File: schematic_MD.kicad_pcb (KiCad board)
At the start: 2 copper layers, 100 x 100 mm, 115 parts, among them J1 XT60, J10 Gate_PWR_Jump, J13 EXPWR_GND, J2 XT60, J3 XT60, J4 CAN_Bus, J5 Rotaly_encoder_1, J6 Rotaly_encoder_2, J7 Z_jumper, J8 Z_jumper, J9 Conn_02x01, Q1 SQJ886EP-T1_GE3, Q2 SQJ886EP-T1_GE3, Q3 SQJ886EP-T1_GE3, Q4 SQJ886EP-T1_GE3, Q5 SQJ886EP-T1_GE3, Q6 SQJ886EP-T1_GE3, Q7 SQJ886EP-T1_GE3, Q8 SQJ886EP-T1_GE3, SW1 SW_MEC_5G, U1 UCC21520DW, U11 74HC04, U2 XC6206P332MR-G, U3 UCC21520DW, U4 UCC21520DW, U5 UCC21520DW, U6 STM32F405RGTx, U7 MAX3051, U8 L78M05ABDT-TR

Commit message: fix drive circuit
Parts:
- added C26: 10u, Capacitor_SMD:C_1210_3225Metric_Pad1.33x2.70mm_HandSolder, F.Cu at (180.1, 55.6)
- added C43: 1uF, Capacitor_SMD:C_0603_1608Metric_Pad1.08x0.95mm_HandSolder, F.Cu at (182.8, 55.6)
- R24, R25, R26, R27, R28, R29, R30, R31: value 10k -> 20k
- moved U11 2.82 mm to (119.8, 98.2)
- moved C13 2.82 mm to (119.5, 103.4)
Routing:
- net Net-(U5-OUTA): track 0.00 -> 32.2 mm, vias 0 -> 2
- net /Driver1/H-bridge_left: track 11.2 -> 26.8 mm, vias 36 -> 37
- net /Driver1/H-bridge_right: track 7.60 -> 22.9 mm, vias 36 -> 37
- net GND2: track 35.5 -> 44.6 mm, vias 2 -> 6
- net Net-(U3-OUTA): track 31.0 -> 32.4 mm
- net /Driver/H-bridge_right: track 25.8 -> 24.7 mm
- net /Driver/H-bridge_left: track 30.4 -> 29.5 mm

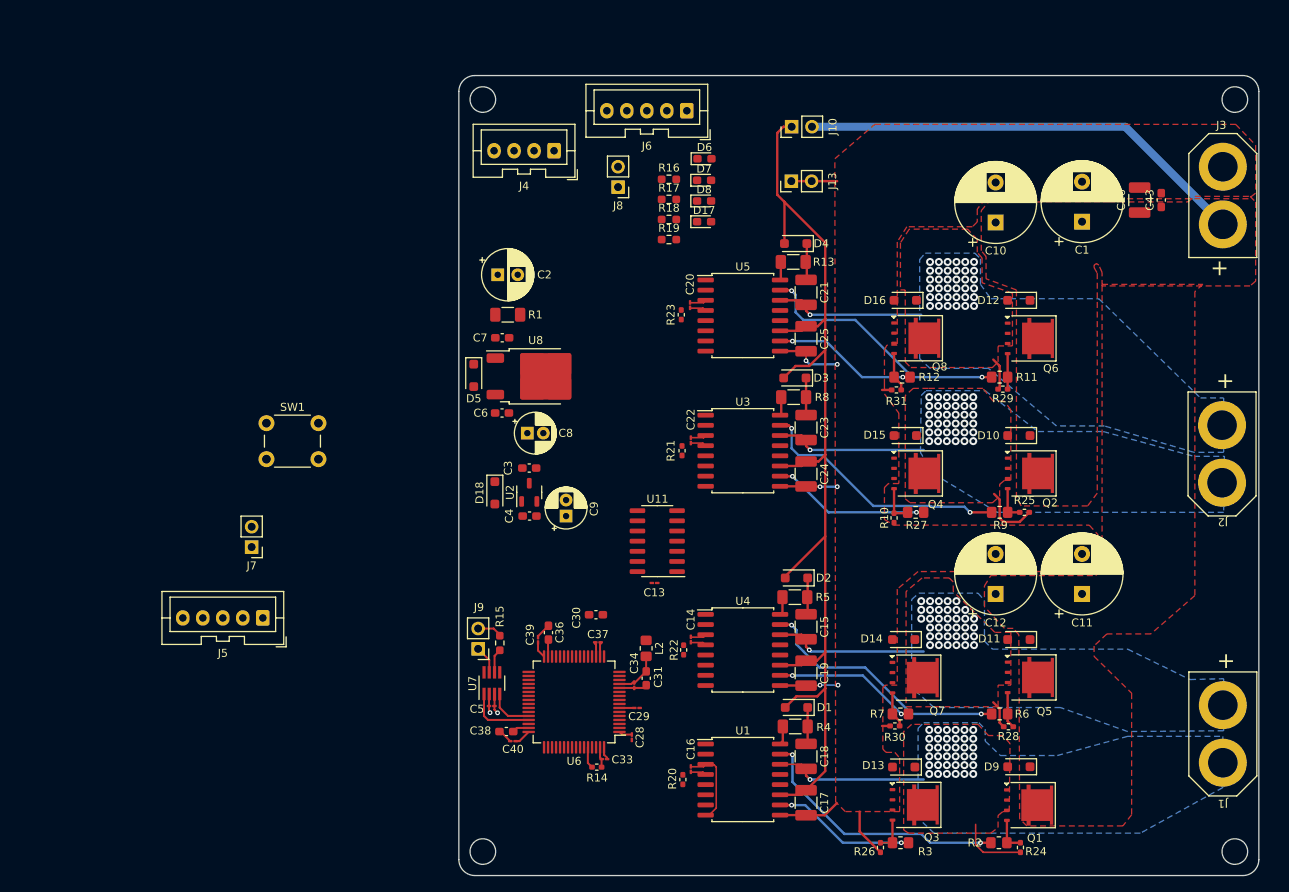
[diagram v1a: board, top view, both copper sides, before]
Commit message: add logic parts
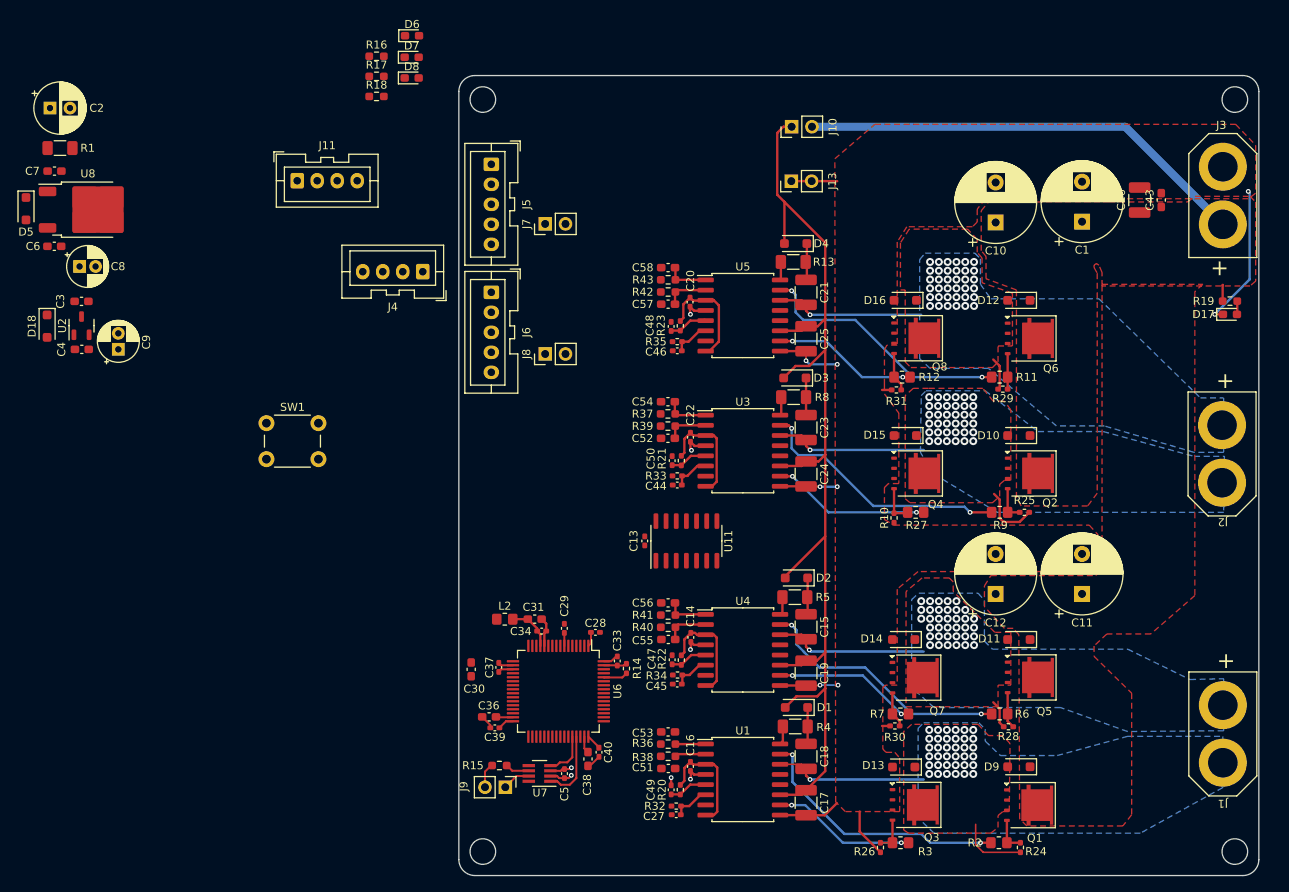
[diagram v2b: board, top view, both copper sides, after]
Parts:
- added C27: 1nF, Capacitor_SMD:C_0402_1005Metric_Pad0.74x0.62mm_HandSolder, F.Cu at (122.2, 132.4)
- added C44: 1nF, Capacitor_SMD:C_0402_1005Metric_Pad0.74x0.62mm_HandSolder, F.Cu at (122.3, 91.2)
- added C45: 1nF, Capacitor_SMD:C_0402_1005Metric_Pad0.74x0.62mm_HandSolder, F.Cu at (122.3, 116.1)
- added C46: 1nF, Capacitor_SMD:C_0402_1005Metric_Pad0.74x0.62mm_HandSolder, F.Cu at (122.3, 74.4)
- added C47: 22nF, Capacitor_SMD:C_0402_1005Metric_Pad0.74x0.62mm_HandSolder, F.Cu at (121.7, 113.0)
- added C48: 22nF, Capacitor_SMD:C_0402_1005Metric_Pad0.74x0.62mm_HandSolder, F.Cu at (121.5, 71.4)
- added C49: 22nF, Capacitor_SMD:C_0402_1005Metric_Pad0.74x0.62mm_HandSolder, F.Cu at (121.5, 129.3)
- added C50: 22nF, Capacitor_SMD:C_0402_1005Metric_Pad0.74x0.62mm_HandSolder, F.Cu at (121.7, 88.1)
- added C51: 33pF, Capacitor_SMD:C_0603_1608Metric_Pad1.08x0.95mm_HandSolder, F.Cu at (121.2, 126.6)
- added C52: 33pF, Capacitor_SMD:C_0603_1608Metric_Pad1.08x0.95mm_HandSolder, F.Cu at (121.1, 85.3)
- added C53: 33pF, Capacitor_SMD:C_0603_1608Metric_Pad1.08x0.95mm_HandSolder, F.Cu at (121.2, 122.0)
- added C54: 33pF, Capacitor_SMD:C_0603_1608Metric_Pad1.08x0.95mm_HandSolder, F.Cu at (121.1, 80.8)
- added C55: 33pF, Capacitor_SMD:C_0603_1608Metric_Pad1.08x0.95mm_HandSolder, F.Cu at (121.2, 110.5)
- added C56: 33pF, Capacitor_SMD:C_0603_1608Metric_Pad1.08x0.95mm_HandSolder, F.Cu at (121.2, 105.9)
- added C57: 33pF, Capacitor_SMD:C_0603_1608Metric_Pad1.08x0.95mm_HandSolder, F.Cu at (121.2, 68.6)
- added C58: 33pF, Capacitor_SMD:C_0603_1608Metric_Pad1.08x0.95mm_HandSolder, F.Cu at (121.2, 64.0)
- added J11: CAN_Bus, Connector_JST:JST_XA_B04B-XASK-1_1x04_P2.50mm_Vertical, F.Cu at (74.8, 53.1)
- added R32: 20k, Resistor_SMD:R_0402_1005Metric_Pad0.72x0.64mm_HandSolder, F.Cu at (122.2, 131.3)
- added R33: 20k, Resistor_SMD:R_0402_1005Metric_Pad0.72x0.64mm_HandSolder, F.Cu at (122.3, 90.0)
- added R34: 20k, Resistor_SMD:R_0402_1005Metric_Pad0.72x0.64mm_HandSolder, F.Cu at (122.3, 114.9)
- added R35: 20k, Resistor_SMD:R_0402_1005Metric_Pad0.72x0.64mm_HandSolder, F.Cu at (122.3, 73.3)
- added R36: 51, Resistor_SMD:R_0603_1608Metric_Pad0.98x0.95mm_HandSolder, F.Cu at (121.2, 123.6)
- added R37: 51, Resistor_SMD:R_0603_1608Metric_Pad0.98x0.95mm_HandSolder, F.Cu at (121.1, 82.3)
- added R38: 51, Resistor_SMD:R_0603_1608Metric_Pad0.98x0.95mm_HandSolder, F.Cu at (121.2, 125.1)
- added R39: 51, Resistor_SMD:R_0603_1608Metric_Pad0.98x0.95mm_HandSolder, F.Cu at (121.1, 83.8)
- added R40: 51, Resistor_SMD:R_0603_1608Metric_Pad0.98x0.95mm_HandSolder, F.Cu at (121.2, 109.0)
- added R41: 51, Resistor_SMD:R_0603_1608Metric_Pad0.98x0.95mm_HandSolder, F.Cu at (121.2, 107.4)
- added R42: 51, Resistor_SMD:R_0603_1608Metric_Pad0.98x0.95mm_HandSolder, F.Cu at (121.2, 67.1)
- added R43: 51, Resistor_SMD:R_0603_1608Metric_Pad0.98x0.95mm_HandSolder, F.Cu at (121.2, 65.5)
- C13, C14, C16, C20, C22, C28, C29, C33, C34, C37, C39, C40, C5: footprint Capacitor_SMD:C_01005_0402Metric_Pad0.57x0.30mm_HandSolder -> Capacitor_SMD:C_0402_1005Metric_Pad0.74x0.62mm_HandSolder
- moved R19 70.5 mm to (191.4, 68.2)
- moved D17 66.7 mm to (191.4, 69.8)
- moved J5 63.5 mm to (99.1, 51.1), turned to -90 degrees
- moved C2 59.7 mm to (43.9, 44.1)
- moved C4 59.7 mm to (47.9, 74.2)
- moved C9 59.7 mm to (52.4, 74.2)
- moved R1 59.7 mm to (45.1, 49.1)
- moved C6 59.7 mm to (44.4, 61.3)
- moved C7 59.7 mm to (44.5, 51.9)
- moved C8 59.7 mm to (47.6, 63.9)
- moved D18 59.7 mm to (43.5, 71.3)
- moved D5 59.7 mm to (40.9, 56.6)
- moved C3 59.7 mm to (47.8, 68.2)
- moved U2 59.7 mm to (47.8, 71.3)
- moved U8 59.7 mm to (48.6, 56.8)
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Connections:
- J4 pad 1: +12V -> GND1
- J4 pad 2: GND1 -> +12V
- U1 pad 1: /Driver/Left_Highside_PWM_IN -> Net-(U1-INA)
- U1 pad 2: /Driver/Left_Lowside_PWM_IN -> Net-(U1-INB)
- U1 pad 6: unconnected-(U1-DT-Pad6) -> Net-(U1-DT)
- U3 pad 1: /Driver1/Left_Highside_PWM_IN -> Net-(U3-INA)
- U3 pad 2: /Driver1/Left_Lowside_PWM_IN -> Net-(U3-INB)
- U3 pad 6: unconnected-(U3-DT-Pad6) -> Net-(U3-DT)
- U4 pad 1: /Driver/Right_Highside_PWM_IN -> Net-(U4-INA)
- U4 pad 2: /Driver/Right_Lowside_PWM_IN -> Net-(U4-INB)
- U4 pad 6: unconnected-(U4-DT-Pad6) -> Net-(U4-DT)
- U5 pad 1: /Driver1/Right_Highside_PWM_IN -> Net-(U5-INA)
- U5 pad 2: /Driver1/Right_Lowside_PWM_IN -> Net-(U5-INB)
- U5 pad 6: unconnected-(U5-DT-Pad6) -> Net-(U5-DT)
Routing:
- net +3.3V: track 27.3 -> 67.7 mm
- net GND2: track 44.6 -> 62.9 mm, vias 6 -> 8
- net GND1: track 21.3 -> 27.2 mm, vias 1 -> 6
- net Net-(U4-INB): track 0.00 -> 5.45 mm
- net Net-(U5-INB): track 0.00 -> 5.42 mm
- net Net-(U3-INA): track 0.00 -> 5.41 mm
- net Net-(U3-INB): track 0.00 -> 5.39 mm
- net Net-(U4-INA): track 0.00 -> 5.36 mm
- net Net-(U5-INA): track 0.00 -> 5.33 mm
- net /Driver1/EN_right: track 0.00 -> 5.04 mm
- net /Driver/EN_right: track 0.00 -> 4.90 mm
- net Net-(U1-DT): track 0.00 -> 4.86 mm
- net /Driver/EN_left: track 0.00 -> 4.83 mm
- net /Driver1/EN_left: track 0.00 -> 4.75 mm
- net Net-(U5-DT): track 0.00 -> 4.63 mm
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
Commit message: update pcb
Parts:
- added Y3: Crystal, Crystal:Crystal_SMD_3225-4Pin_3.2x2.5mm, F.Cu at (105.3, 101.0)
- added Y4: Crystal, Crystal:Crystal_SMD_3215-2Pin_3.2x1.5mm, F.Cu at (110.4, 80.4)
- moved C6 67.6 mm to (111.9, 57.5)
- moved C7 67.6 mm to (112.0, 48.1)
- moved D5 67.6 mm to (108.4, 52.8)
- moved U8 67.6 mm to (116.1, 52.9)
- moved R1 67.6 mm to (112.7, 46.1)
- moved D18 65.8 mm to (108.9, 63.4)
- moved C4 64.5 mm to (111.8, 66.1)
- moved U2 64.5 mm to (111.8, 63.2)
- moved C3 64.5 mm to (111.8, 60.3)
- moved C2 62.7 mm to (106.6, 46.2), turned to 90 degrees
- moved C8 61.1 mm to (108.4, 58.1), turned to 180 degrees
- moved C9 60.5 mm to (112.8, 69.9), turned to 180 degrees
- moved J9 54.3 mm to (110.7, 75.6), turned to 90 degrees
- moved J6 51.3 mm to (99.1, 118.4)
- moved J7 51.3 mm to (105.8, 109.9)
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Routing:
- net Net-(J11-Pin_3): track 3.04 -> 23.1 mm
- net Net-(J11-Pin_4): track 3.58 -> 18.2 mm
- net +3.3V: track 67.7 -> 70.5 mm
- net Net-(U6-BOOT0): track 3.06 -> 1.89 mm

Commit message: fix logic
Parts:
- removed J7, J8: Z_jumper, Connector_PinHeader_2.54mm:PinHeader_1x02_P2.54mm_Vertical
- removed Y3: Crystal, Crystal:Crystal_SMD_3225-4Pin_3.2x2.5mm
- added C32: 18pF, Capacitor_SMD:C_0603_1608Metric, F.Cu at (98.7, 91.6)
- added C35: 18pF, Capacitor_SMD:C_0603_1608Metric, F.Cu at (104.6, 91.6)
- added C41: 20pF, Capacitor_SMD:C_0603_1608Metric, F.Cu at (105.7, 70.1)
- added C42: 20pF, Capacitor_SMD:C_0603_1608Metric, F.Cu at (108.7, 70.1)
- added Y1: 25MHz, Crystal:Crystal_SMD_3225-4Pin_3.2x2.5mm, F.Cu at (101.6, 91.6)
- moved C4 54.8 mm to (57.1, 64.9)
- moved C6 54.8 mm to (57.2, 56.3)
- moved C7 54.8 mm to (57.2, 46.9)
- moved C8 54.8 mm to (53.7, 56.9)
- moved D18 54.8 mm to (54.2, 62.2)
- moved D5 54.8 mm to (53.7, 51.6)
- moved U8 54.8 mm to (61.4, 51.7)
- moved C2 54.8 mm to (51.9, 45.0)
- moved C3 54.8 mm to (57.1, 59.1)
- moved C9 54.8 mm to (58.0, 68.7)
- moved R1 54.8 mm to (58.0, 44.9)
- moved U2 54.8 mm to (57.1, 62.0)
- moved C5 31.5 mm to (78.2, 58.4)
- moved J9 31.5 mm to (85.6, 56.7)
- moved R15 31.5 mm to (86.3, 59.4)
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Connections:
- J5 pad 1: unconnected-(J5-Pin_1-Pad1) -> GND1
- J5 pad 4: Net-(J5-Pin_4) -> unconnected-(J5-Pin_4-Pad4)
- J5 pad 5: GND1 -> unconnected-(J5-Pin_5-Pad5)
- J6 pad 1: unconnected-(J6-Pin_1-Pad1) -> GND1
- J6 pad 4: Net-(J6-Pin_4) -> unconnected-(J6-Pin_4-Pad4)
- J6 pad 5: GND1 -> unconnected-(J6-Pin_5-Pad5)
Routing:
- net GND1: track 27.5 -> 57.6 mm, vias 6 -> 8
- net (no net): track 0.00 -> 21.8 mm
- net Net-(J11-Pin_3): track 23.1 -> 5.07 mm
- net Net-(J11-Pin_4): track 18.2 -> 3.51 mm
- net Net-(U6-PH0): track 0.00 -> 8.28 mm
- net Net-(U6-PB14): track 0.00 -> 6.30 mm
- net Net-(U6-PB15): track 0.00 -> 6.26 mm
- net Net-(U6-PH1): track 0.00 -> 5.83 mm

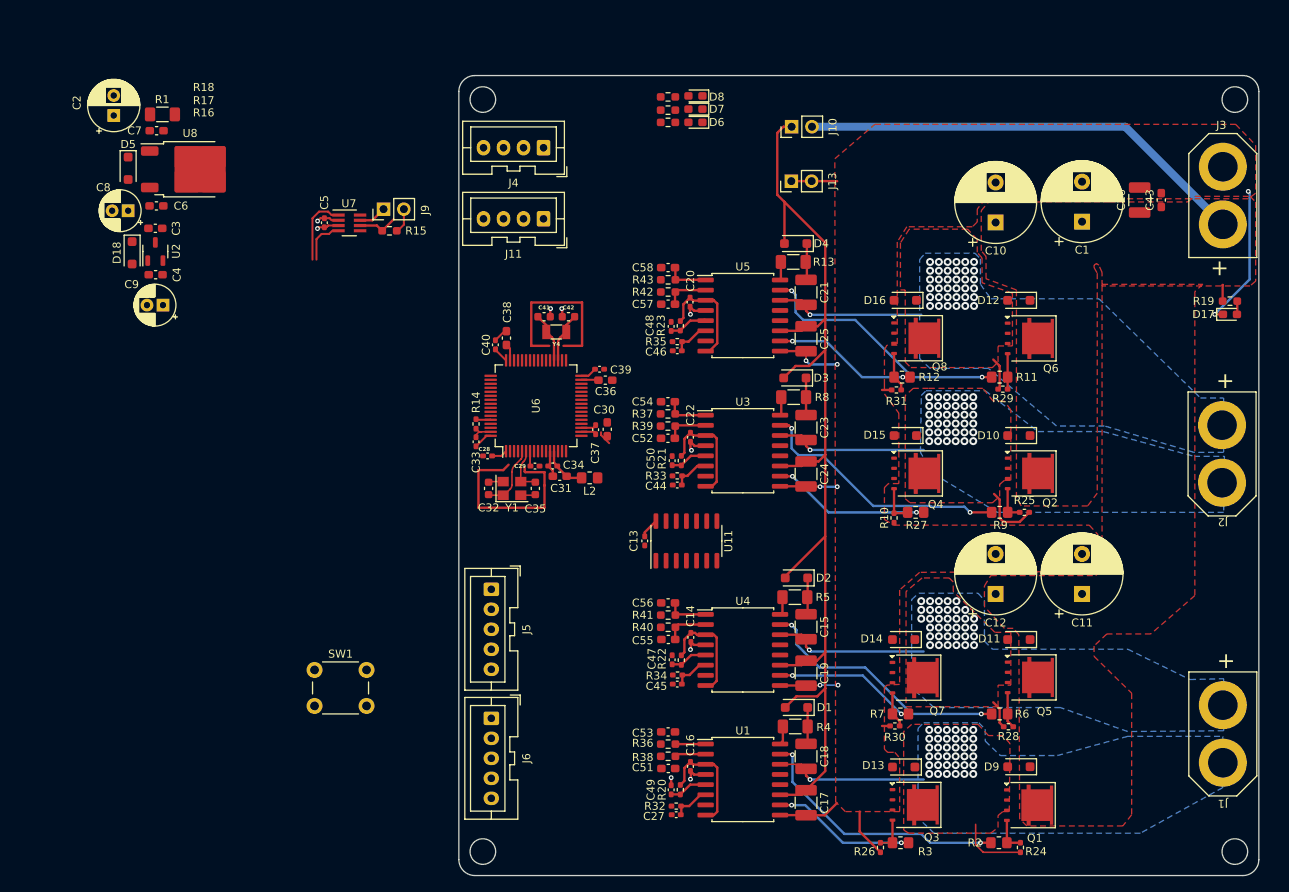
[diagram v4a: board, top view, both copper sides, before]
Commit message: logic design update
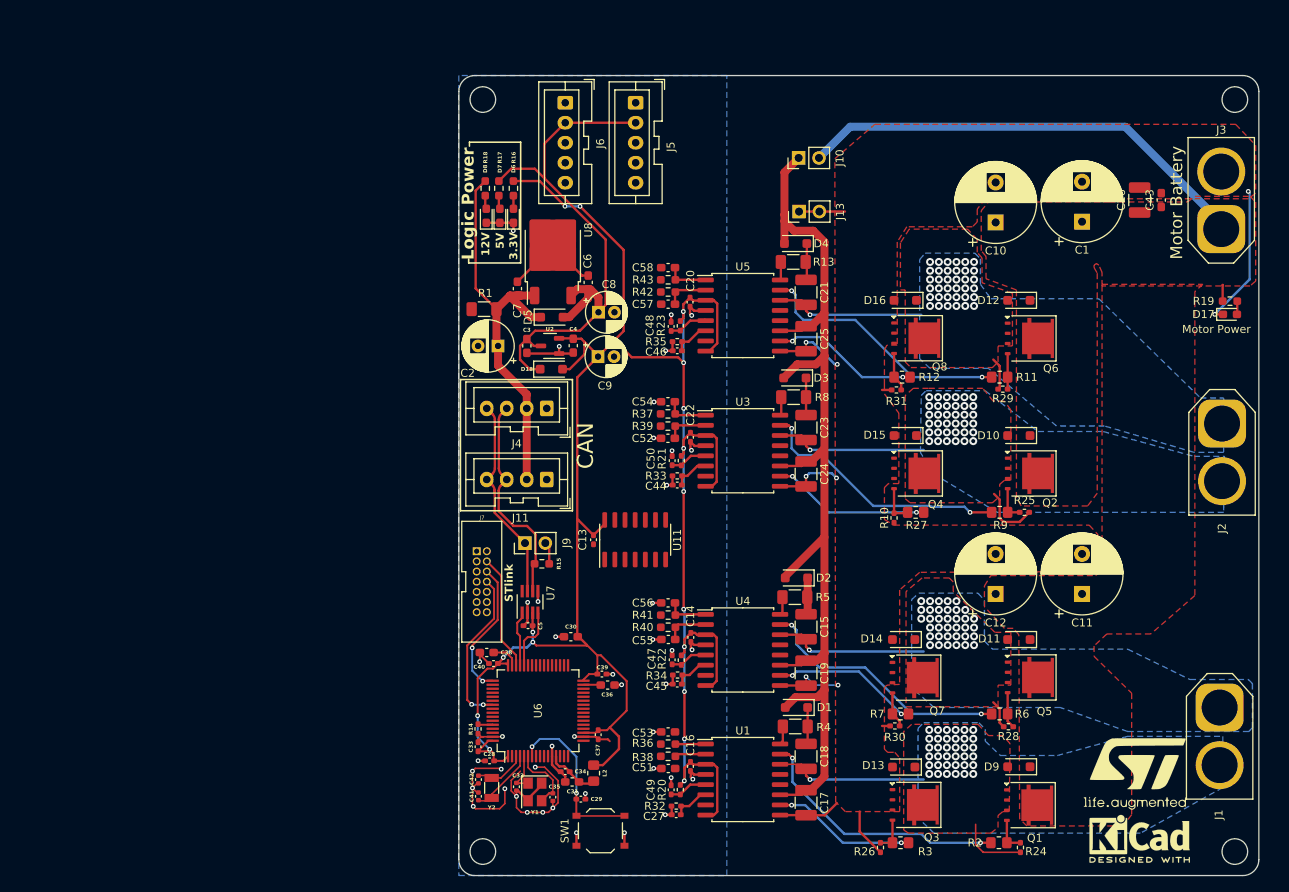
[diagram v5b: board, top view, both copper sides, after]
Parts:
- removed Y4: Crystal, Crystal:Crystal_SMD_3215-2Pin_3.2x1.5mm
- added G***: LOGO, RDC_footprint:STM_logo_25mm, F.Cu at (179.5, 127.3)
- added J7: Conn_02x07_Odd_Even, RDC_footprint:JTAG_box_connector, F.Cu at (97.9, 112.2)
- added REF**: KiCad-Logo2_5mm_SilkScreen, Symbol:KiCad-Logo2_5mm_SilkScreen, F.Cu at (180.1, 135.4)
- added Y2: Crystal, Crystal:Crystal_SMD_3215-2Pin_3.2x1.5mm, F.Cu at (99.1, 129.1)
- C32, C35, C41, C42: footprint Capacitor_SMD:C_0603_1608Metric -> Capacitor_SMD:C_0402_1005Metric
- J1, J2: footprint RDC_footprint:XT60 -> Connector_AMASS:AMASS_XT60-F_1x02_P7.20mm_Vertical
- J3: footprint RDC_footprint:XT60 -> Connector_AMASS:AMASS_XT60-M_1x02_P7.20mm_Vertical
- SW1: footprint Button_Switch_THT:SW_PUSH_6mm -> Button_Switch_SMD:SW_Push_1P1T_XKB_TS-1187A
- moved J6 77.5 mm to (108.3, 43.4)
- moved J5 63.4 mm to (117.1, 43.4)
- moved C41 60.5 mm to (97.5, 130.1), turned to 90 degrees
- moved C8 60.1 mm to (112.5, 69.6), turned to 0 degrees
- moved C42 58.9 mm to (97.5, 128.0), turned to -90 degrees
- moved C5 56.4 mm to (103.7, 108.8), turned to 180 degrees
- moved D5 56.1 mm to (106.6, 70.2), turned to 0 degrees
- moved C2 56.0 mm to (99.9, 73.8), turned to 180 degrees
- moved C6 54.8 mm to (111.2, 65.9), turned to 90 degrees
- moved C9 54.8 mm to (112.4, 75.1), turned to 0 degrees
- moved D18 54.4 mm to (106.6, 76.7), turned to 0 degrees
- moved C4 53.0 mm to (109.3, 73.8), turned to -90 degrees
- moved U7 52.5 mm to (103.9, 105.8), turned to 90 degrees
- moved U2 50.7 mm to (106.4, 73.8), turned to 180 degrees
- moved C7 49.2 mm to (102.3, 66.6), turned to 90 degrees
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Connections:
- C29 pad 1: Net-(U6-NRST) -> /STM32F405/NRST
- C41 pad 1: Net-(U6-PB15) -> Net-(U6-PC15)
- C42 pad 1: Net-(U6-PB14) -> Net-(U6-PC14)
- SW1 pad 2: GND1 -> /STM32F405/NRST
- U11 pad 10: GND1 -> /Driver1/Left_Lowside_PWM_IN
- U11 pad 11: GND1 -> /Driver1/Left_Highside_PWM_IN
- U11 pad 12: GND1 -> /Driver1/Right_Lowside_PWM_IN
- U11 pad 13: GND1 -> /Driver1/Right_Highside_PWM_IN
- U11 pad 5: /Driver1/Left_Highside_PWM_IN -> GND1
- U11 pad 6: /Driver1/Left_Lowside_PWM_IN -> GND1
- U11 pad 8: /Driver1/Right_Lowside_PWM_IN -> GND1
- U11 pad 9: /Driver1/Right_Highside_PWM_IN -> GND1
- U6 pad 3: unconnected-(U6-PC14-Pad3) -> Net-(U6-PC14)
- U6 pad 35: Net-(U6-PB14) -> unconnected-(U6-PB14-Pad35)
- U6 pad 36: Net-(U6-PB15) -> unconnected-(U6-PB15-Pad36)
- U6 pad 4: unconnected-(U6-PC15-Pad4) -> Net-(U6-PC15)
- U6 pad 7: Net-(U6-NRST) -> /STM32F405/NRST
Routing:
- net +3.3V: track 70.8 -> 278.1 mm, vias 1 -> 17
- net +5V: track 0.00 -> 73.7 mm
- net GND1: track 57.6 -> 118.7 mm, vias 8 -> 43
- net +12V: track 0.00 -> 51.4 mm
- net Net-(J11-Pin_4): track 3.51 -> 26.3 mm
- net Net-(J11-Pin_3): track 5.07 -> 27.2 mm
- net (no net): track 21.8 -> 0.00 mm
- net /STM32F405/NRST: track 0.00 -> 21.6 mm, vias 0 -> 2
- net /STM32F405/SWO: track 0.00 -> 20.0 mm, vias 0 -> 2
- net /STM32F405/SWCLK: track 0.00 -> 17.4 mm, vias 0 -> 2
- net /STM32F405/SWDIO: track 0.00 -> 14.5 mm
- net Net-(U6-PC15): track 0.00 -> 8.77 mm
- net Net-(U6-PC14): track 0.00 -> 6.76 mm
- net Net-(U6-PB14): track 6.30 -> 0.00 mm
- net Net-(U6-PB15): track 6.26 -> 0.00 mm
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- added copper zone on B.Cu, net GND1
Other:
- board text added: "12V"
- board text added: "3.3V"
- board text added: "5V"
- board text added: "CAN"
- board text added: "Logic Power"
- board text added: "Motor Battery"
- board text added: "Motor Power"
- board text added: "STlink"
